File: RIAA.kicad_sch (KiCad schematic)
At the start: 46 parts, among them K1 G6K-2, P8 Fra Hovedprint, P9 Fra Ledning, U1 LM833, U2 LM833, U3 LM7812_TO220, U4 LM7912_TO220

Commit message: feat: updated schematics.
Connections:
- net GND LF is gone; now on net GND: K1.3, K1.4, K1.5, K1.6, P9.5 (Pin_5)
- net 31V renamed 30V
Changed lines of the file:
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@@
 	(wire
 		(pts
-			(xy 326.39 176.53) (xy 326.39 193.04)
+			(xy 326.39 168.91) (xy 326.39 193.04)
 		)
 		(stroke
@@
 		)
 	)
-	(global_label "GND PSU"
+	(global_label "GND MB"
 		(shape input)
 		(at 173.99 162.56 270)
@@
 		)
 		(property "Intersheetrefs" "${INTERSHEET_REFS}"
-			(at 173.99 174.1933 90)
+			(at 173.99 173.1047 90)
 			(effects
 				(font
@@
 		)
 	)
-	(global_label "GND LF"
+	(global_label "GND"
 		(shape input)
 		(at 241.3 208.28 270)
@@
 		)
 		(property "Intersheetrefs" "${INTERSHEET_REFS}"
-			(at 241.3 218.22 90)
+			(at 241.3 215.1357 90)
 			(effects
 				(font
@@
 	(global_label "21V"
 		(shape input)
-		(at 326.39 176.53 90)
+		(at 326.39 168.91 90)
 		(fields_autoplaced yes)
 		(effects
@@
 		)
 		(property "Intersheetrefs" "${INTERSHEET_REFS}"
-			(at 326.39 170.0372 90)
+			(at 326.39 162.4172 90)
 			(effects
 				(font
@@
 		)
 	)
-	(global_label "31V"
+	(global_label "30V"
 		(shape input)
 		(at 34.29 149.86 180)
@@
 		)
 	)
-	(global_label "GND LF"
+	(global_label "GND"
 		(shape input)
 		(at 231.14 208.28 270)
@@
 		)
 		(property "Intersheetrefs" "${INTERSHEET_REFS}"
-			(at 231.14 218.22 90)
+			(at 231.14 215.1357 90)
 			(effects
 				(font
@@
 		)
 	)
-	(global_label "GND LF"
+	(global_label "GND"
 		(shape input)
 		(at 243.84 185.42 90)
@@
 		)
 		(property "Intersheetrefs" "${INTERSHEET_REFS}"
-			(at 243.84 175.48 90)
+			(at 243.84 178.5643 90)
 			(effects
 				(font
@@
 		)
 	)
-	(global_label "GND LF"
+	(global_label "GND"
 		(shape input)
 		(at 233.68 185.42 90)
@@
 		)
 		(property "Intersheetrefs" "${INTERSHEET_REFS}"
-			(at 233.68 175.48 90)
+			(at 233.68 178.5643 90)
 			(effects
 				(font
@@
 		)
 	)
-	(global_label "GND PSU"
+	(global_label "GND MB"
 		(shape input)
 		(at 34.29 195.58 180)
@@
 		)
 		(property "Intersheetrefs" "${INTERSHEET_REFS}"
-			(at 22.6567 195.58 0)
+			(at 23.7453 195.58 0)
 			(effects
 				(font
@@
 		)
 	)
-	(global_label "GND PSU"
+	(global_label "GND MB"
 		(shape input)
 		(at 312.42 190.5 90)
@@
 		)
 		(property "Intersheetrefs" "${INTERSHEET_REFS}"
-			(at 312.42 178.8667 90)
+			(at 312.42 179.9553 90)
 			(effects
 				(font
@@
 		)
 	)
-	(global_label "GND LF"
+	(global_label "GND"
 		(shape input)
 		(at 365.76 172.72 90)
@@
 		)
 		(property "Intersheetrefs" "${INTERSHEET_REFS}"
-			(at 365.76 162.78 90)
+			(at 365.76 165.8643 90)
 			(effects
 				(font
@@
 		)
 	)
-	(global_label "31V"
+	(global_label "30V"
 		(shape input)
 		(at 328.93 190.5 90)

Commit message: feat: updated schematics.
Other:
- note added: "Relay Notes - G6K P1 to D2 cathode - G6K P2 to P8-6 (R OUT RIAA) & P9-3 (R OUT) - G6K P3 to P9-5 (GND) - G6K P4 to P9-5 (GND) - G6K P5 to P9-5 (GND) - G6K P6 to P9-5 (GND) - G6K P7 to P8-4 (L OUT RIAA) & P9-1 (L OUT) - G6K P8 to D2 anode"
- note removed: "Relay Notes - G6K P1 to D2 cathode - G6K P2 to P8-6 (R OUT RIAA) & P9-3 (R OUT) - G6K P3 to P9-5 (GND LF) - G6K P4 to P9-5 (GND LF) - G6K P5 to P9-5 (GND LF) - G6K P6 to P9-5 (GND LF) - G6K P7 to P8-4 (L OUT RUAA) & P9-1 (L OUT) - G6K P8 to D2 anode"
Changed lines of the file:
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@@
 		)
 	)
-	(text "Relay Notes\n- G6K P1 to D2 cathode\n- G6K P2 to P8-6 (R OUT RIAA) & P9-3 (R OUT)\n- G6K P3 to P9-5 (GND LF)\n- G6K P4 to P9-5 (GND LF)\n- G6K P5 to P9-5 (GND LF)\n- G6K P6 to P9-5 (GND LF)\n- G6K P7 to P8-4 (L OUT RUAA) & P9-1 (L OUT)\n- G6K P8 to D2 anode\n\n"
+	(text "Relay Notes\n- G6K P1 to D2 cathode\n- G6K P2 to P8-6 (R OUT RIAA) & P9-3 (R OUT)\n- G6K P3 to P9-5 (GND)\n- G6K P4 to P9-5 (GND)\n- G6K P5 to P9-5 (GND)\n- G6K P6 to P9-5 (GND)\n- G6K P7 to P8-4 (L OUT RIAA) & P9-1 (L OUT)\n- G6K P8 to D2 anode\n\n"
 		(exclude_from_sim no)
 		(at 238.252 139.192 0)

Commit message: feat: updated schematics.
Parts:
- removed C18, C19: 220uF, Capacitor_THT:CP_Radial_D8.0mm_P3.50mm, symbol Device:C_Polarized_Small
- removed C6, C7: 0.22uF, Capacitor_THT:C_Disc_D7.5mm_W2.5mm_P5.00mm, symbol Device:C
- removed U3: LM7812_TO220, Package_TO_SOT_THT:TO-220-3_Vertical, symbol Regulator_Linear:LM7812_TO220
- removed U4: LM7912_TO220, Package_TO_SOT_THT:TO-220-3_Vertical, symbol Regulator_Linear:LM7912_TO220
- added U3: LM7824_TO220, Package_TO_SOT_THT:TO-220-3_Horizontal_TabDown, symbol Regulator_Linear:LM7824_TO220
- C1, C10, C11, C13, C14, C15, C4, C5, C8, C9: footprint Capacitor_THT:C_Disc_D7.5mm_W2.5mm_P5.00mm -> Capacitor_THT:C_Rect_L4.6mm_W3.0mm_P2.50mm_MKS02_FKP02
- C16: footprint Capacitor_THT:CP_Radial_D8.0mm_P3.50mm -> Capacitor_THT:CP_Radial_D8.0mm_P5.00mm
- C2: value 220uF -> 330uF; footprint Capacitor_THT:CP_Radial_D8.0mm_P3.50mm -> Capacitor_THT:CP_Radial_D12.5mm_P5.00mm
- C3: value 220uF -> 100uF; footprint Capacitor_THT:CP_Radial_D8.0mm_P3.50mm -> Capacitor_THT:CP_Radial_D12.5mm_P5.00mm
- D1, D2: footprint Diode_THT:D_5W_P10.16mm_Horizontal -> Diode_THT:D_A-405_P10.16mm_Horizontal
- RV1: footprint Potentiometer_SMD:Potentiometer_ACP_CA6-VSMD_Vertical -> Potentiometer_SMD:Potentiometer_ACP_CA6-VSMD_Vertical_Hole
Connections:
- net GND CHASSIS is gone; now on net 24VDC-: BC549.3 (E), C2.2, P8.2 (Pin_2), P8.3 (Pin_3), P9.6 (Pin_6), R17.1
- net 30V: now also C2.1, U3.1 (VI)
- net GND: no longer C2.1, C3.2
- net +15V renamed 24VDC+
- net 24VDC+: now also U3.3 (VO)
- net -15V renamed 24VDC-
- net 24VDC-: now also C3.2, U3.2 (GND)

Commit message: feat: updated schematics.
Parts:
- removed C13: 39nF, Capacitor_THT:C_Rect_L4.6mm_W3.0mm_P2.50mm_MKS02_FKP02, symbol Device:C
- removed C3: 100uF, Capacitor_THT:CP_Radial_D12.5mm_P5.00mm, symbol Device:C_Polarized_Small
- removed C4: 33nF, Capacitor_THT:C_Rect_L4.6mm_W3.0mm_P2.50mm_MKS02_FKP02, symbol Device:C
- removed C8: 2uF, Capacitor_THT:C_Rect_L4.6mm_W3.0mm_P2.50mm_MKS02_FKP02, symbol Device:C
- removed R10: 499, Resistor_THT:R_Axial_DIN0204_L3.6mm_D1.6mm_P7.62mm_Horizontal, symbol Device:R
- removed R3: 54.9k, Resistor_THT:R_Axial_DIN0204_L3.6mm_D1.6mm_P7.62mm_Horizontal, symbol Device:R
- removed unit 2 of U1
- removed unit 1 of U1
- removed U2: LM833, Package_SO:SOIC-8_3.9x4.9mm_P1.27mm, symbol Amplifier_Operational:LM358
- removed U3: LM7824_TO220, Package_TO_SOT_THT:TO-220-3_Horizontal_TabDown, symbol Regulator_Linear:LM7824_TO220
- added C12, C17: 10nF, Capacitor_THT:C_Rect_L4.6mm_W3.0mm_P2.50mm_MKS02_FKP02, symbol Device:C
- added C16: 2n7, Capacitor_THT:C_Rect_L4.6mm_W3.0mm_P2.50mm_MKS02_FKP02, symbol Device:C
- added C2, C4: 220uF, Capacitor_THT:CP_Radial_D12.5mm_P5.00mm, symbol Device:C_Polarized_Small
- added C6: 10uF, Capacitor_THT:CP_Radial_D12.5mm_P5.00mm, symbol Device:C_Polarized_Small
- added C7: 2200uF, Capacitor_THT:CP_Radial_D12.5mm_P5.00mm, symbol Device:C_Polarized_Small
- added C9: 100nF, Capacitor_THT:C_Rect_L4.6mm_W3.0mm_P2.50mm_MKS02_FKP02, symbol Device:C
- added D1, D2: 1N4002, Diode_THT:D_A-405_P10.16mm_Horizontal, symbol Device:D_Zener
- added U2: LM317_TO-220, Package_TO_SOT_THT:TO-220-3_Horizontal_TabDown, symbol Regulator_Linear:LM317_TO-220
- added U3: OPA2134, symbol Amplifier_Operational:OPA2134
- C1: value 200uF -> 10nF
- C10: value 39nF -> 10nF
- C11: value 200uF -> 2n7
- C14: value 33nF -> 10nF
- C15: value 2uF -> 10nF
- C3: renamed from C2; value 330uF -> 0.1uF
- C5: value 1nF -> 10nF
- C8: renamed from C9; value 1nF -> 10nF
- R1: value 499 -> 4370
- R11: value 80.6k -> 47k
- R12: value 8.45k -> 470k
- R13: value 2.47 -> 330k
- R14: value 54.9k -> 100
- R15: value 2k -> 330k
- R16: value 4.3k -> 27k
- R2: value 47k -> 240
- R4: value 2k -> 470k
- R5: value 4.3k -> 330k
- R6: value 2.47 -> 100
- R7: value 8.45k -> 330k
- R8: value 80.6k -> 27k
- U1: value LM833 -> OPA2134
- renumbered BC549 to BC1, C16 to C13, D2 to D3, D1 to D4, P8 to P1, P9 to P2, R18 to R10, R9 to R3, R17 to R9
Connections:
- net 24VDC+: now also C1.2, R2.1, C2.1, C7.1, C9.2, D1.1 (K), D2.1 (K), U2.2 (VO)
- net 24VDC-: now also C5.2, R1.2, C4.1, C6.2, C7.2, C9.1
- net 30V: now also D1.2 (A), U2.3 (VI)
- net GND: now also C1.1, C5.1, R12.2, C2.2, C4.2; no longer C1.2, C11.2, C14.2, C5.2, C8.2, R14.2, R15.2, R2.2, R3.2
- net L IN  PICKUP: now also C14.2, R11.1; no longer C5.1, R2.1
- net L OUT: now also C17.1; no longer R16.1
- net R IN  PICKUP: now also C8.2; no longer C8.1
- net R OUT: now also C12.1; no longer R5.1
- net at R11.2: now also R13.2
- net at C11.1: now also R8.2, C12.2, U3.7
- net at R6.1: now also R5.1, U3.6 (-)
- net at R5.2: now also R3.2; no longer R4.1
- net at R7.2, R8.1: now also C10.1, C11.2; no longer C10.2
- net at R12.1: now also C14.1, U3.3 (+); no longer R13.2
- net at R15.1: now also C15.2, R14.2; no longer R16.2
- net at R14.1: now also R13.1, U3.2 (-); no longer C15.2
- net at R6.2, R7.1: now also C10.2
- new net: C6.1, D2.2 (A), R1.1, R2.2, U2.1 (ADJ)
- new net: C15.1, C16.2, R15.2, R16.1
- new net: C16.1, C17.2, R16.2, U3.1
- new net: C8.1, R4.1, U3.5 (+)
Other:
- moved on the sheet: BC1, C13, C3, C8, D3, D4, K1, P1, P2, R10, R3, R9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

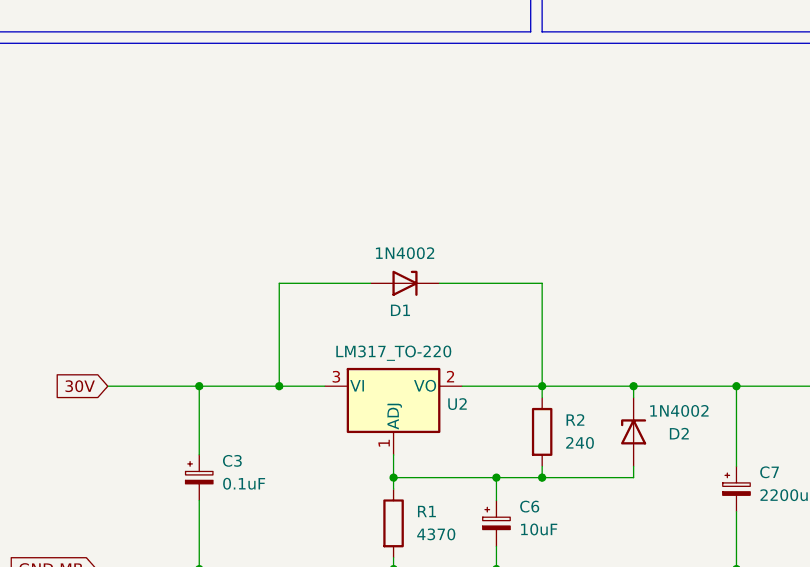
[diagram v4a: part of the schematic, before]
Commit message: feat: reversed D1.
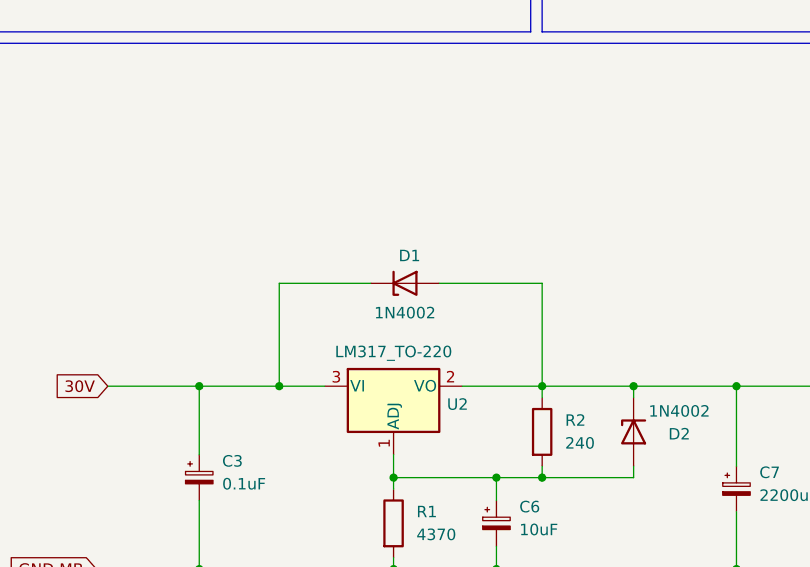
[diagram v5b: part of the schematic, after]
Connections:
- net 24VDC+: now also D1.2 (A); no longer D1.1 (K)
- net 30V: now also D1.1 (K); no longer D1.2 (A)
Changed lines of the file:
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@@
 		(lib_id "Device:D_Zener")
 		(at 101.6 134.62 0)
-		(mirror y)
+		(mirror x)
 		(unit 1)
 		(exclude_from_sim no)
@@
 		(dnp no)
 		(property "Reference" "D1"
-			(at 101.092 137.668 0)
+			(at 102.108 131.572 0)
 			(effects
 				(font
@@
 		)
 		(property "Value" "1N4002"
-			(at 101.6 131.318 0)
+			(at 101.6 137.922 0)
 			(effects
 				(font

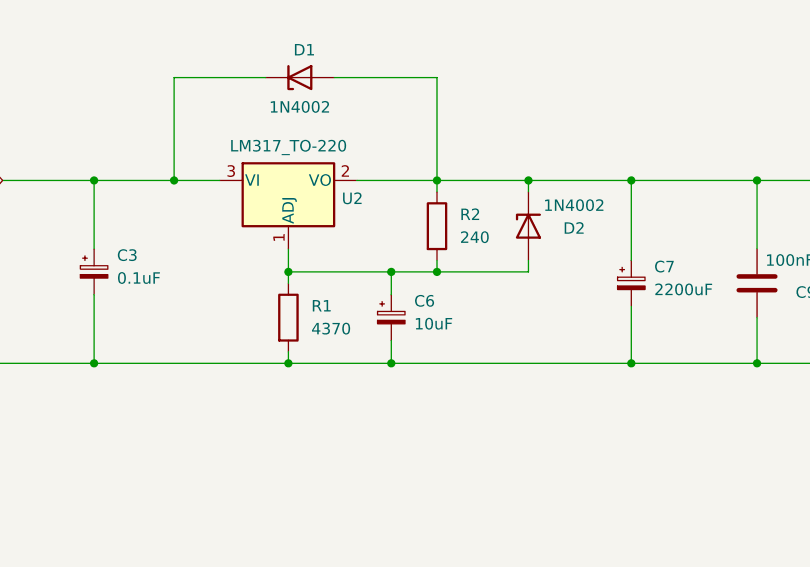
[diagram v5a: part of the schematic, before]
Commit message: feat: Updated PSU resistor values.
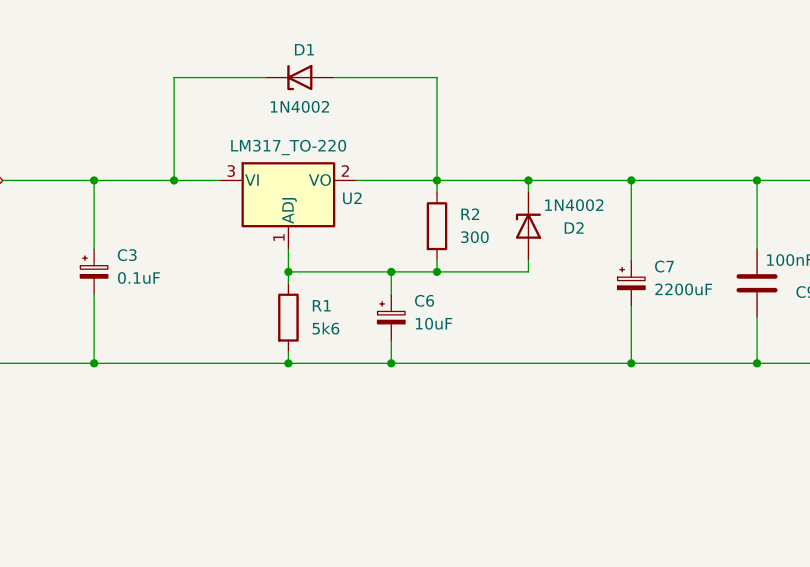
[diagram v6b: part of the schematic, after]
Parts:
- R1: value 4370 -> 5k6
- R2: value 240 -> 300
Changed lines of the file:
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@@
 			)
 		)
-		(property "Value" "4370"
+		(property "Value" "5k6"
 			(at 102.87 162.5599 0)
 			(effects
@@
 			)
 		)
-		(property "Value" "240"
+		(property "Value" "300"
 			(at 119.38 152.3999 0)
 			(effects

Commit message: feat: Updated PCB.
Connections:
- net GND: now also R11.2, R13.2, R3.2, R5.2
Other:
- moved on the sheet: C10, C11, C12, C14, C15, C16, C17, C8, R11, R12, R13, R14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

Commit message: WIP
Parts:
- U3: footprint (none) -> OPA2134:D8
- renumbered U1 to U3
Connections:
- net L IN  PICKUP is gone; now on net L IN PICKUP: C14.2, R11.1
- net R IN  PICKUP is gone; now on net R IN PICKUP: C8.2, R3.1
- net GND: now also BC1.3 (E), C3.2, C6.2, C7.2, C9.1, P1.2 (Pin_2), P1.3 (Pin_3), P2.6 (Pin_6), R1.2, R9.1
- removed net 24VDC-: BC1.3 (E), C3.2, C4.1, C5.2, C6.2, C7.2, C9.1, P1.2 (Pin_2), P1.3 (Pin_3), P2.6 (Pin_6), R1.2, R9.1, U3.4 (V-)
- new net: C4.1, C5.2, U3.4 (V-)
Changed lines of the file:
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@@
 	)
 	(junction
-		(at 340.36 165.1)
+		(at 278.13 78.74)
 		(diameter 0)
 		(color 0 0 0 0)
 	)
 	(junction
-		(at 228.6 133.35)
+		(at 340.36 165.1)
 		(diameter 0)
 		(color 0 0 0 0)
 	)
 	(junction
-		(at 278.13 78.74)
+		(at 228.6 133.35)
 		(diameter 0)
 		(color 0 0 0 0)
@@
 	)
 	(junction
-		(at 72.39 85.09)
-		(diameter 0)
-		(color 0 0 0 0)
-	)
-	(junction
 		(at 248.92 160.02)
 		(diameter 0)
@@
 	(wire
 		(pts
-			(xy 72.39 85.09) (xy 72.39 86.36)
-		)
-		(stroke
-			(width 0)
-			(type default)
-		)
-	)
-	(wire
-		(pts
 			(xy 146.05 91.44) (xy 146.05 92.71)
 		)
@@
 	(wire
 		(pts
+			(xy 275.59 78.74) (xy 278.13 78.74)
+		)
+		(stroke
+			(width 0)
+			(type default)
+		)
+	)
+	(wire
+		(pts
 			(xy 196.85 121.92) (xy 196.85 133.35)
 		)
@@
 	(wire
 		(pts
-			(xy 72.39 82.55) (xy 72.39 85.09)
-		)
-		(stroke
-			(width 0)
-			(type default)
-		)
-	)
-	(wire
-		(pts
 			(xy 185.42 52.07) (xy 181.61 52.07)
 		)
@@
 	(wire
 		(pts
-			(xy 275.59 78.74) (xy 278.13 78.74)
+			(xy 207.01 52.07) (xy 214.63 52.07)
 		)
 		(stroke
@@
 	(wire
 		(pts
-			(xy 207.01 52.07) (xy 214.63 52.07)
+			(xy 214.63 133.35) (xy 210.82 133.35)
 		)
 		(stroke
@@
 	(wire
 		(pts
-			(xy 214.63 133.35) (xy 210.82 133.35)
+			(xy 278.13 78.74) (xy 280.67 78.74)
 		)
 		(stroke
@@
 	(wire
 		(pts
-			(xy 278.13 78.74) (xy 280.67 78.74)
+			(xy 220.98 133.35) (xy 219.71 133.35)
 		)
 		(stroke
@@
 	(wire
 		(pts
-			(xy 220.98 133.35) (xy 219.71 133.35)
+			(xy 72.39 82.55) (xy 72.39 85.09)
 		)
 		(stroke
@@
 		)
 	)
-	(global_label "24VDC-"
-		(shape input)
-		(at 72.39 86.36 270)
-		(fields_autoplaced yes)
-		(effects
-			(font
-				(size 1.27 1.27)
-			)
-			(justify right)
-		)
-		(property "Intersheetrefs" "${INTERSHEET_REFS}"
-			(at 72.39 96.9652 90)
-			(effects
-				(font
-					(size 1.27 1.27)
-				)
-				(justify right)
-				(hide yes)
-			)
-		)
-	)
 	(global_label "GND"
 		(shape input)
@@
 		)
 	)
-	(global_label "24VDC-"
+	(global_label "GND"
 		(shape input)
 		(at 162.56 166.37 0)
@@
 		)
 		(property "Intersheetrefs" "${INTERSHEET_REFS}"
-			(at 173.1652 166.37 0)
+			(at 169.4157 166.37 0)
 			(effects
 				(font
@@
 		)
 	)
-	(global_label "L IN  PICKUP"
+	(global_label "L IN PICKUP"
 		(shape input)
 		(at 135.89 78.74 180)
@@
 		)
 		(property "Intersheetrefs" "${INTERSHEET_REFS}"
-			(at 120.0233 78.74 0)
+			(at 120.9909 78.74 0)
 			(effects
 				(font
@@
 		)
 	)
-	(global_label "R IN  PICKUP"
+	(global_label "R IN PICKUP"
 		(shape input)
 		(at 275.59 78.74 180)
@@
 		)
 		(property "Intersheetrefs" "${INTERSHEET_REFS}"
-			(at 259.4814 78.74 0)
+			(at 260.449 78.74 0)
 			(effects
 				(font
@@
 		(dnp no)
 		(fields_autoplaced yes)
-		(property "Reference" "U1"
-			(at 74.93 73.6599 0)
+		(property "Reference" "U3"
+			(at 73.66 73.6599 0)
 			(effects
 				(font
@@
 		)
 		(property "Value" "OPA2134"
-			(at 74.93 76.1999 0)
+			(at 73.66 76.1999 0)
 			(effects
 				(font
@@
 			(project "RIAA"
 				(path "/d42afdab-200b-47bd-9783-ae2fad19e73b"
-					(reference "U1")
+					(reference "U3")
 					(unit 3)
 				)
@@
 			)
 		)
-		(property "Footprint" ""
+		(property "Footprint" "OPA2134:D8"
 			(at 182.88 81.28 0)
 			(effects
@@
 			)
 		)
-		(property "Footprint" ""
+		(property "Footprint" "OPA2134:D8"
 			(at 314.96 81.28 0)
 			(effects
